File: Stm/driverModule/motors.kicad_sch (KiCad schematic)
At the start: 27 parts, among them J1 Conn_02x05_Odd_Even, Q1 BSS138, Q2 BSS138, Q3 AON7410, U1 TLE94103EP, U201 DRV8838, U204 VNH5019A-E

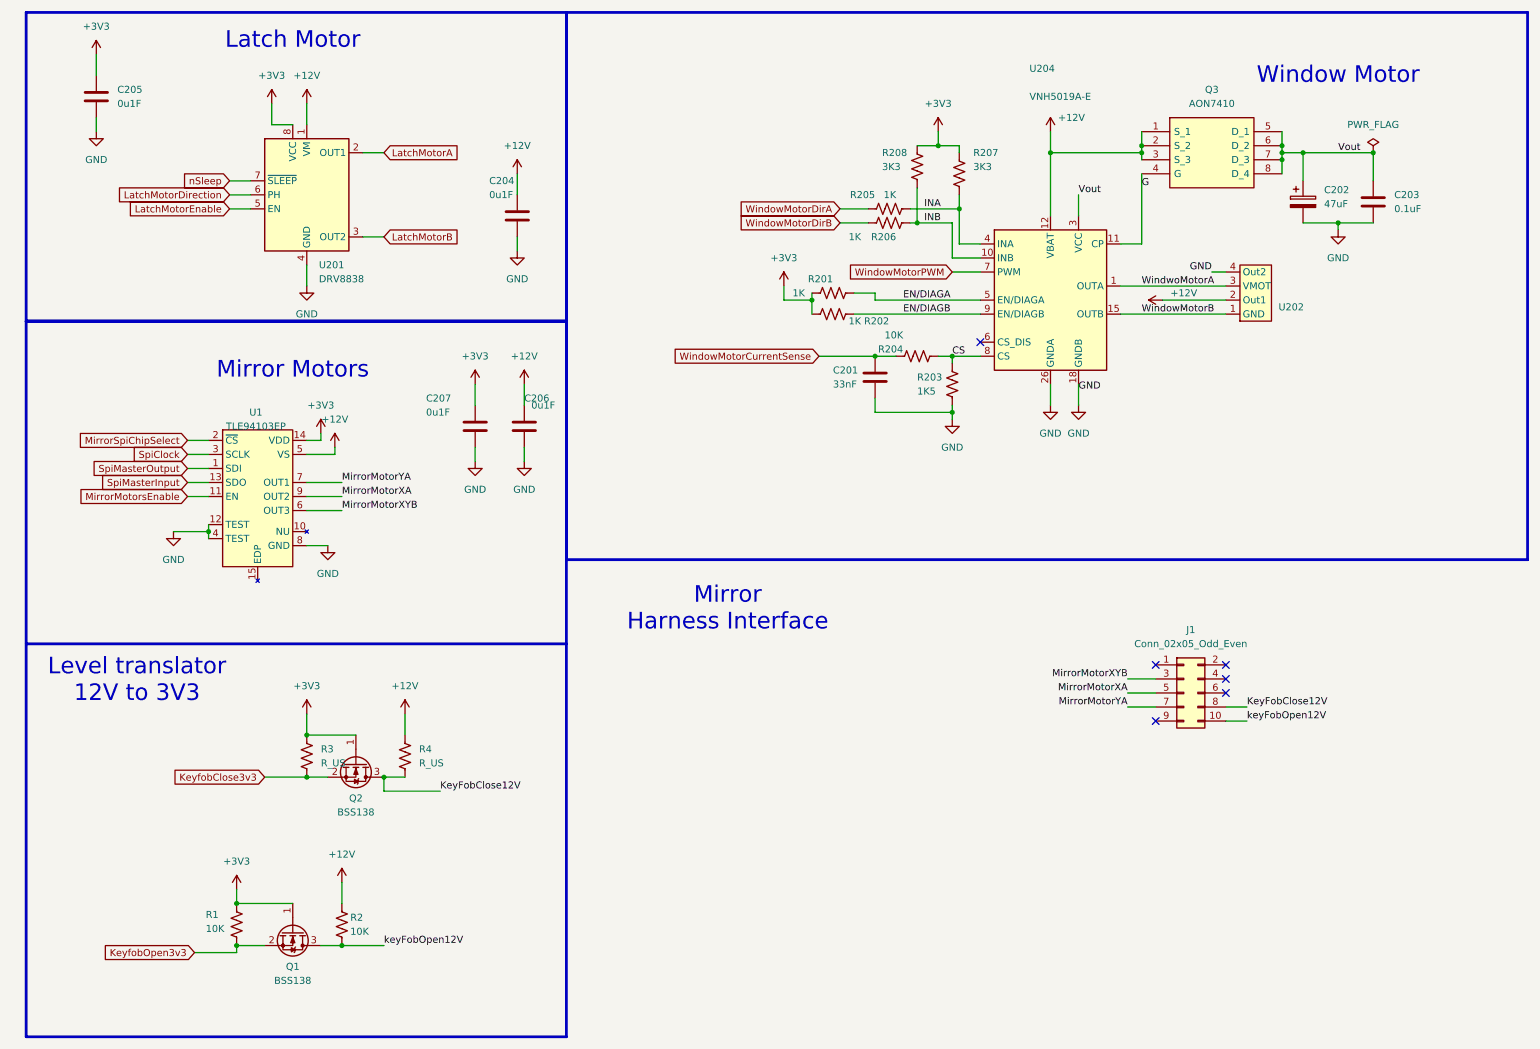
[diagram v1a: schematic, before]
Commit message: Driver Board
Modify driver module for the PCI express cpu card
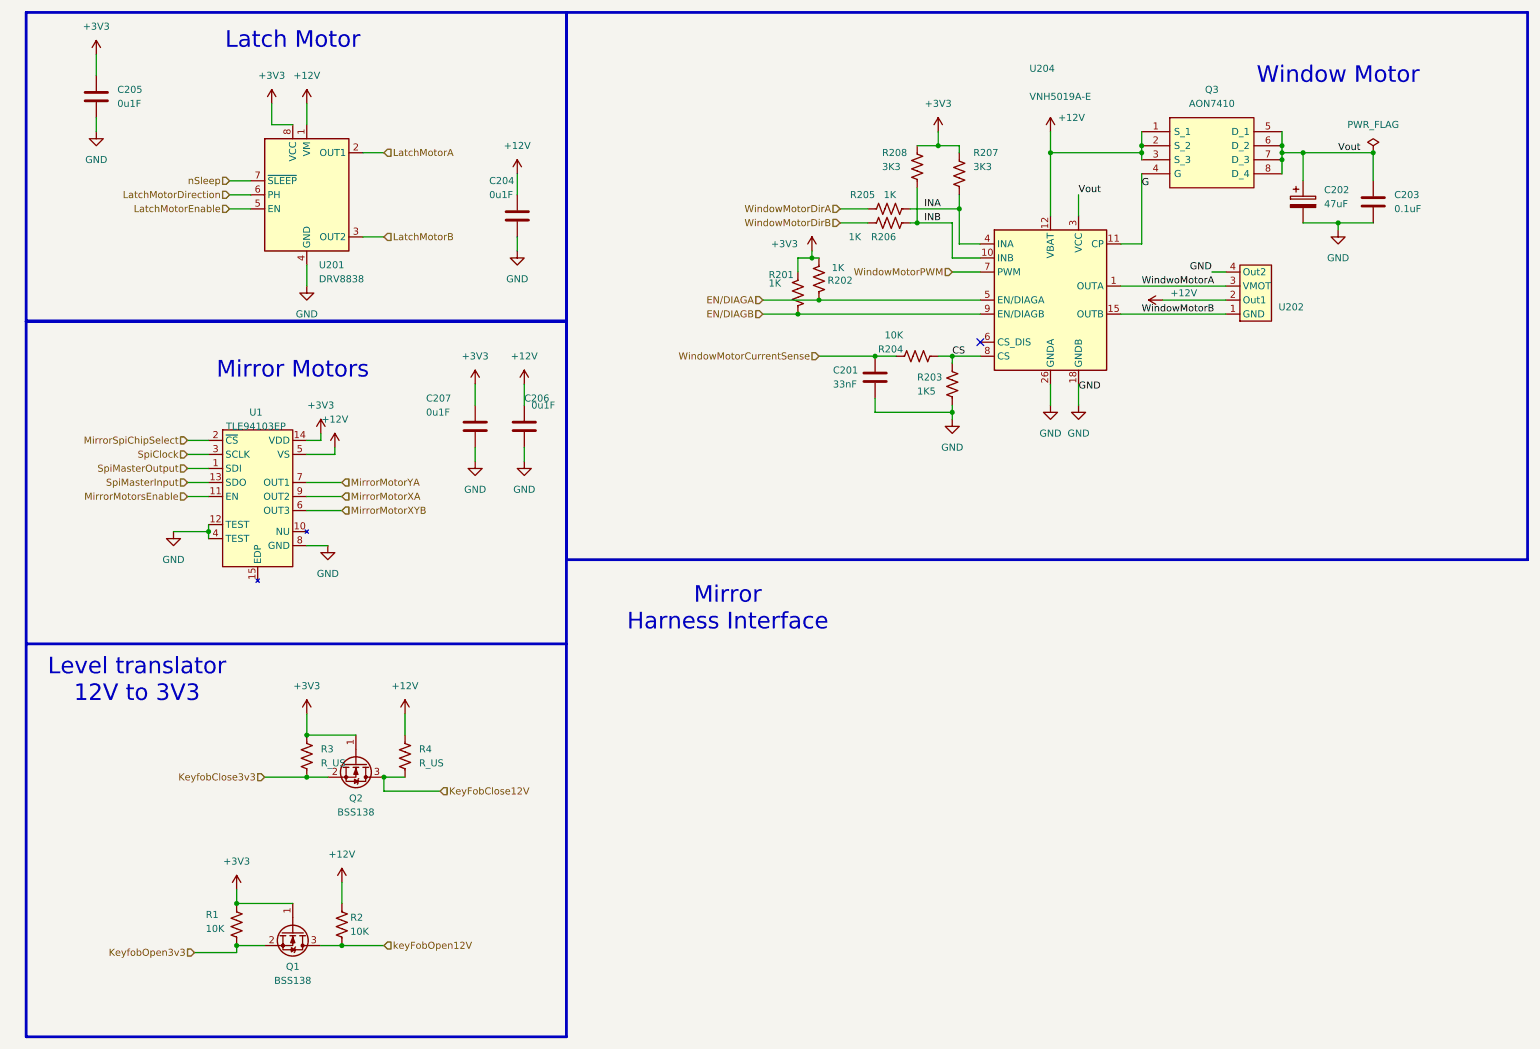
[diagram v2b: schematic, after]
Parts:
- removed J1: Conn_02x05_Odd_Even, Connector_PinHeader_2.54mm:PinHeader_2x05_P2.54mm_Vertical, symbol Connector_Generic:Conn_02x05_Odd_Even
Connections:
- net EN/DIAGA: now also R202.2; no longer R201.2
- net EN/DIAGB: now also R201.2; no longer R202.2
- no-connect marks 6 -> 1
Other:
- moved on the sheet: R201, R202

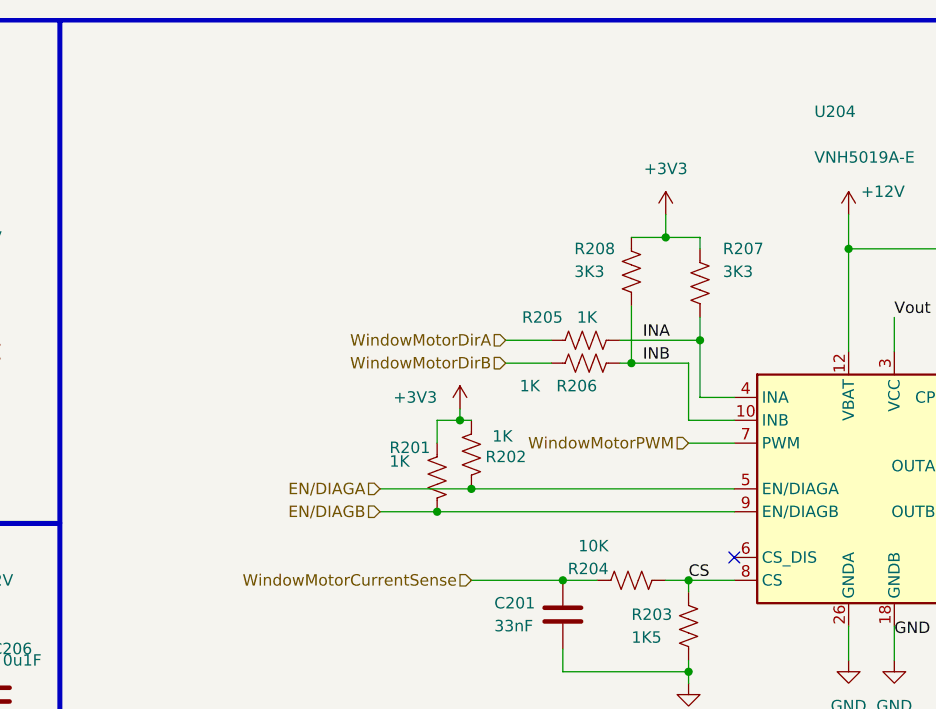
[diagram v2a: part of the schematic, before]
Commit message: Connector
Connect all missing inputs and outputs
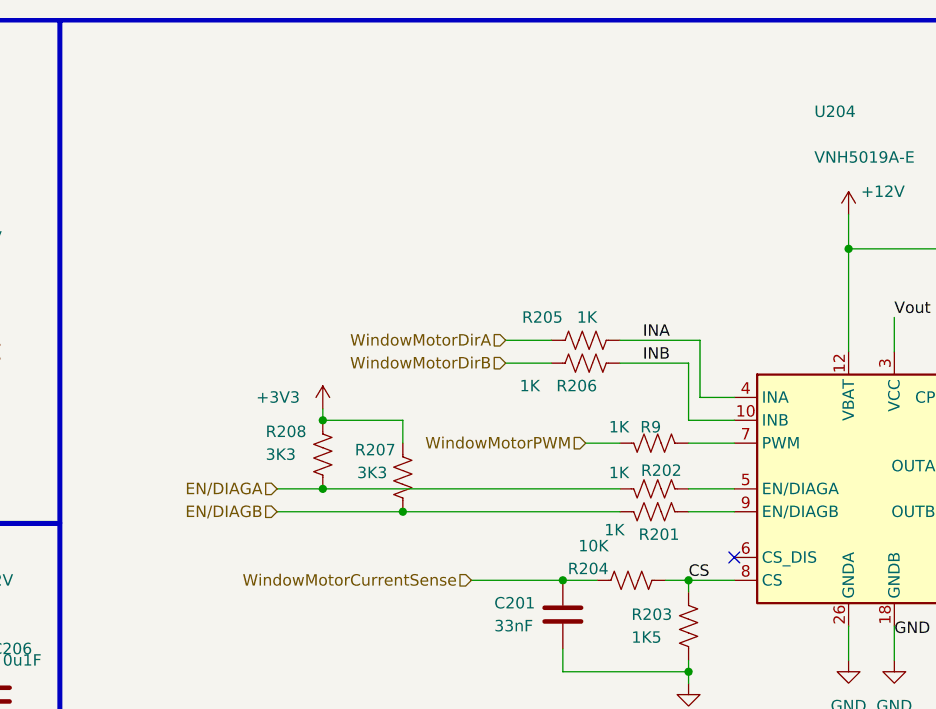
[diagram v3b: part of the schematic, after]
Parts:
- added R9: 1K, Resistor_SMD:R_0402_1005Metric_Pad0.72x0.64mm_HandSolder, symbol Device:R_US
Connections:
- net +3V3: no longer R201.1, R202.1
- net EN/DIAGA: now also R202.1, R208.2; no longer R202.2, U204.5 (EN/DIAGA)
- net EN/DIAGB: now also R201.1, R207.2; no longer R201.2, U204.9 (EN/DIAGB)
- net INA: no longer R207.2
- net INB: no longer R208.2
- net WindowMotorPWM: now also R9.1; no longer U204.7 (PWM)
- new net: R9.2, U204.7 (PWM)
- new net: R201.2, U204.9 (EN/DIAGB)
- new net: R202.2, U204.5 (EN/DIAGA)
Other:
- moved on the sheet: R201, R202, R207, R208

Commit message: Connectors
Remove some enable signals
Added Harness connectors
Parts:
- removed R207: 3K3, Resistor_SMD:R_0402_1005Metric_Pad0.72x0.64mm_HandSolder, symbol Device:R_US
- removed U202: ~, Local_Footprints:HeaderMotorCustomeSMD, symbol Local_symbols:HeaderForCustomMotorConnector
- added R11, R13: 10K, Resistor_SMD:R_0402_1005Metric_Pad0.72x0.64mm_HandSolder, symbol Device:R_US
- added U2: 74LVC2G04, Package_TO_SOT_SMD:SOT-363_SC-70-6, symbol 74xGxx:74LVC2G04
- C202: footprint Capacitor_SMD:CP_Elec_6.3x5.4_Nichicon -> Capacitor_Tantalum_SMD:CP_EIA-6032-15_Kemet-U
- Q3: footprint Local_Footprints:DFN_3X3_EP -> User_Footprint:DFN_3X3_EP
- R9: value 1K -> 10K
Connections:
- net EN/DIAGB is gone; now on net WindownMotorEnable: R201.1
- net WindowMotorPWM is gone; now on net +3V3: R9.1
- net +3V3: now also R11.1, R13.1, U2.5 (VCC)
- net GND: now also U2.2 (GND)
- net EN/DIAGA renamed WindownMotorEnable
- net MirrorMotorsEnable renamed Enable
- net Enable: now also R11.2
- net WindowMotorDirA: no longer names the net of R205.1
- net WindowMotorDirA: now also U2.6
- net WindowMotorDirB renamed WindowMotorDir
- net WindowMotorDir: now also U2.1
- net WindwoMotorA renamed WindowMotorA
- net nSleep: no longer names the net of U201.7 (~{SLEEP})
- net nSleep: now also R13.2
- no-connect marks 1 -> 3
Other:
- note removed: "Mirror Harness Interface"
- moved on the sheet: C201, C202, C203, Q3, R201, R202, R203, R204, R205, R206, R208, R9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

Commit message: Small modifications
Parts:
- added TP10: TestPoint_Small, TestPoint:TestPoint_Pad_1.0x1.0mm, symbol Connector:TestPoint_Small
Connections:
- net Enable: now also U2.4, TP10.1; no longer R11.2
- net MirrorSpiChipSelect: now also R11.2, U2.3
- no-connect marks 3 -> 1
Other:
- moved on the sheet: R11, U2B
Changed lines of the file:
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@@
 	)
 	(junction
+		(at 50.8 121.92)
+		(diameter 0)
+		(color 0 0 0 0)
+	)
+	(junction
 		(at 63.5 151.13)
 		(diameter 0)
@@
 	)
 	(junction
+		(at 43.18 90.17)
+		(diameter 0)
+		(color 0 0 0 0)
+	)
+	(junction
 		(at 238.76 69.85)
 		(diameter 0)
@@
 		(at 184.15 104.14)
 	)
-	(no_connect
-		(at 161.29 49.53)
-	)
-	(no_connect
-		(at 133.35 49.53)
-	)
 	(wire
 		(pts
@@
 	(wire
 		(pts
+			(xy 50.8 121.92) (xy 52.07 121.92)
+		)
+		(stroke
+			(width 0)
+			(type default)
+		)
+	)
+	(wire
+		(pts
 			(xy 101.6 53.34) (xy 101.6 55.88)
 		)
@@
 	(wire
 		(pts
-			(xy 85.09 121.92) (xy 90.17 121.92)
+			(xy 76.2 124.46) (xy 81.28 124.46)
 		)
 		(stroke
@@
 	(wire
 		(pts
+			(xy 50.8 121.92) (xy 50.8 124.46)
+		)
+		(stroke
+			(width 0)
+			(type default)
+		)
+	)
+	(wire
+		(pts
 			(xy 213.36 69.85) (xy 213.36 71.12)
 		)
@@
 	(wire
 		(pts
+			(xy 46.99 121.92) (xy 50.8 121.92)
+		)
+		(stroke
+			(width 0)
+			(type default)
+		)
+	)
+	(wire
+		(pts
 			(xy 238.76 68.58) (xy 238.76 69.85)
 		)
@@
 	(wire
 		(pts
+			(xy 43.18 85.09) (xy 43.18 90.17)
+		)
+		(stroke
+			(width 0)
+			(type default)
+		)
+	)
+	(wire
+		(pts
 			(xy 179.07 116.84) (xy 179.07 118.11)
 		)
@@
 	(wire
 		(pts
+			(xy 19.05 119.38) (xy 19.05 85.09)
+		)
+		(stroke
+			(width 0)
+			(type default)
+		)
+	)
+	(wire
+		(pts
 			(xy 36.83 48.26) (xy 53.34 48.26)
 		)
@@
 	(wire
 		(pts
+			(xy 43.18 90.17) (xy 45.72 90.17)
+		)
+		(stroke
+			(width 0)
+			(type default)
+		)
+	)
+	(wire
+		(pts
 			(xy 87.63 153.67) (xy 77.47 153.67)
 		)
@@
 	(wire
 		(pts
+			(xy 19.05 85.09) (xy 43.18 85.09)
+		)
+		(stroke
+			(width 0)
+			(type default)
+		)
+	)
+	(wire
+		(pts
 			(xy 154.94 99.06) (xy 165.1 99.06)
 		)
@@
 	(wire
 		(pts
+			(xy 46.99 119.38) (xy 46.99 121.92)
+		)
+		(stroke
+			(width 0)
+			(type default)
+		)
+	)
+	(wire
+		(pts
 			(xy 176.53 106.68) (xy 179.07 106.68)
 		)
@@
 	(wire
 		(pts
-			(xy 85.09 111.76) (xy 85.09 114.3)
+			(xy 76.2 114.3) (xy 76.2 116.84)
 		)
 		(stroke
@@
 	(wire
 		(pts
-			(xy 87.63 111.76) (xy 85.09 111.76)
+			(xy 78.74 114.3) (xy 76.2 114.3)
 		)
 		(stroke
@@
 	(wire
 		(pts
-			(xy 41.91 90.17) (xy 45.72 90.17)
+			(xy 41.91 90.17) (xy 43.18 90.17)
 		)
 		(stroke
@@
 		)
 	)
+	(label "MirrorSpiChipSelect"
+		(at 81.28 124.46 0)
+		(effects
+			(font
+				(size 1.27 1.27)
+			)
+			(justify left bottom)
+		)
+	)
 	(label "INA"
 		(at 173.99 80.01 0)
@@
 	)
 	(label "Enable"
-		(at 90.17 121.92 0)
+		(at 52.07 121.92 0)
 		(effects
 			(font
@@
 	(symbol
 		(lib_id "power:+3V3")
-		(at 87.63 111.76 0)
+		(at 78.74 114.3 0)
 		(unit 1)
 		(exclude_from_sim no)
@@
 		(fields_autoplaced yes)
 		(property "Reference" "#PWR014"
-			(at 87.63 115.57 0)
+			(at 78.74 118.11 0)
 			(effects
 				(font
@@
 		)
 		(property "Value" "+3V3"
-			(at 87.63 106.68 0)
+			(at 78.74 109.22 0)
 			(effects
 				(font
@@
 		)
 		(property "Footprint" ""
-			(at 87.63 111.76 0)
+			(at 78.74 114.3 0)
 			(effects
 				(font
@@
 		)
 		(property "Datasheet" ""
-			(at 87.63 111.76 0)
+			(at 78.74 114.3 0)
 			(effects
 				(font
@@
 		)
 		(property "Description" "Power symbol creates a global label with name \"+3V3\""
-			(at 87.63 111.76 0)
+			(at 78.74 114.3 0)
 			(effects
 				(font
@@
 	)
 	(symbol
+		(lib_id "Connector:TestPoint_Small")
+		(at 50.8 124.46 0)
+		(unit 1)
+		(exclude_from_sim no)
+		(in_bom yes)
+		(on_board yes)
+		(dnp no)
+		(fields_autoplaced yes)
+		(property "Reference" "TP10"
+			(at 52.07 124.4599 0)
+			(effects
+				(font
+					(size 1.27 1.27)
+				)
+				(justify left)
+			)
+		)
+		(property "Value" "TestPoint_Small"
+			(at 52.07 125.7299 0)
+			(effects
+				(font
+					(size 1.27 1.27)
+				)
+				(justify left)
+				(hide yes)
+			)
+		)
+		(property "Footprint" "TestPoint:TestPoint_Pad_1.0x1.0mm"
+			(at 55.88 124.46 0)
+			(effects
+				(font
+					(size 1.27 1.27)
+				)
+				(hide yes)
+			)
+		)
+		(property "Datasheet" "~"
+			(at 55.88 124.46 0)
+			(effects
+				(font
+					(size 1.27 1.27)
+				)
+				(hide yes)
+			)
+		)
+		(property "Description" "test point"
+			(at 50.8 124.46 0)
+			(effects
+				(font
+					(size 1.27 1.27)
+				)
+				(hide yes)
+			)
+		)
+		(pin "1"
+		)
+		(instances
+			(project "driverModule"
+				(path "/959b66be-b3e0-42f8-ad58-f1baefc5b565/929fc890-f6da-48d5-a213-781ba4c4fd4e"
+					(reference "TP10")
+					(unit 1)
+				)
+			)
+		)
+	)
+	(symbol
 		(lib_id "Device:R_US")
-		(at 85.09 118.11 0)
+		(at 76.2 120.65 0)
 		(unit 1)
 		(exclude_from_sim no)
@@
 		(dnp no)
 		(property "Reference" "R11"
-			(at 78.74 115.57 0)
+			(at 69.85 118.11 0)
 			(effects
 				(font
@@
 		)
 		(property "Value" "10K"
-			(at 78.74 118.11 0)
+			(at 69.85 120.65 0)
 			(effects
 				(font
@@
 		)
 		(property "Footprint" "Resistor_SMD:R_0402_1005Metric_Pad0.72x0.64mm_HandSolder"
-			(at 86.106 118.364 90)
+			(at 77.216 120.904 90)
 			(effects
 				(font
@@
 		)
 		(property "Datasheet" "~"
-			(at 85.09 118.11 0)
+			(at 76.2 120.65 0)
 			(effects
 				(font
@@
 		)
 		(property "Description" "Resistor, US symbol"
-			(at 85.09 118.11 0)
+			(at 76.2 120.65 0)
 			(effects
 				(font
@@
 	(symbol
 		(lib_id "74xGxx:74LVC2G04")
-		(at 148.59 49.53 0)
+		(at 34.29 119.38 0)
 		(unit 2)
 		(exclude_from_sim no)
@@
 		(fields_autoplaced yes)
 		(property "Reference" "U2"
-			(at 147.32 38.1 0)
+			(at 33.02 107.95 0)
 			(effects
 				(font
@@
 		)
 		(property "Value" "74LVC2G04"
-			(at 147.32 40.64 0)
+			(at 33.02 110.49 0)
 			(effects
 				(font
@@
 		)
 		(property "Footprint" "Package_TO_SOT_SMD:SOT-363_SC-70-6"
-			(at 148.59 49.53 0)
+			(at 34.29 119.38 0)
 			(effects
 				(font
@@
 		)
 		(property "Datasheet" "http://www.ti.com/lit/sg/scyt129e/scyt129e.pdf"
-			(at 148.59 49.53 0)
+			(at 34.29 119.38 0)
 			(effects
 				(font
@@
 		)
 		(property "Description" "Dual NOT Gate, Low-Voltage CMOS"
-			(at 148.59 49.53 0)
+			(at 34.29 119.38 0)
 			(effects
 				(font
